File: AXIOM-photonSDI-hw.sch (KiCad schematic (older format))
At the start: 4 parts, among them J101 Conn_Coaxial, J102 Conn_Coaxial, J103 Conn_Coaxial, J104 Conn_Coaxial

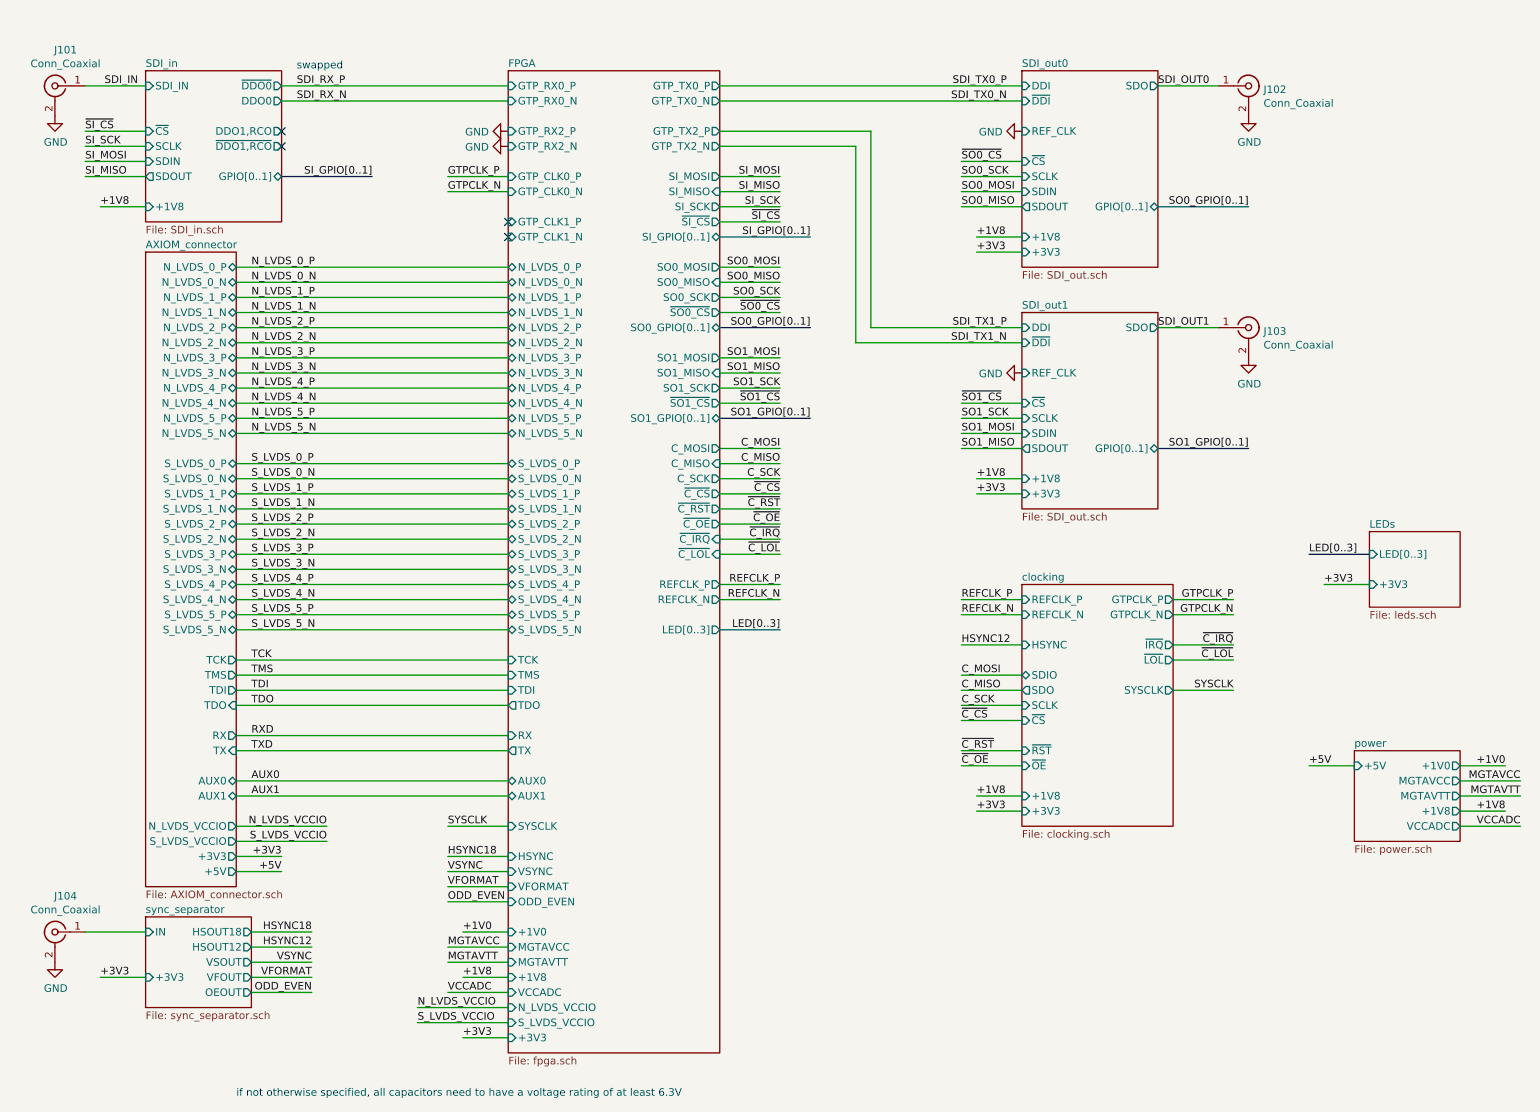
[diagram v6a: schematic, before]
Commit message: fix moved plane bug, add init, done and power enable signals and optimize design
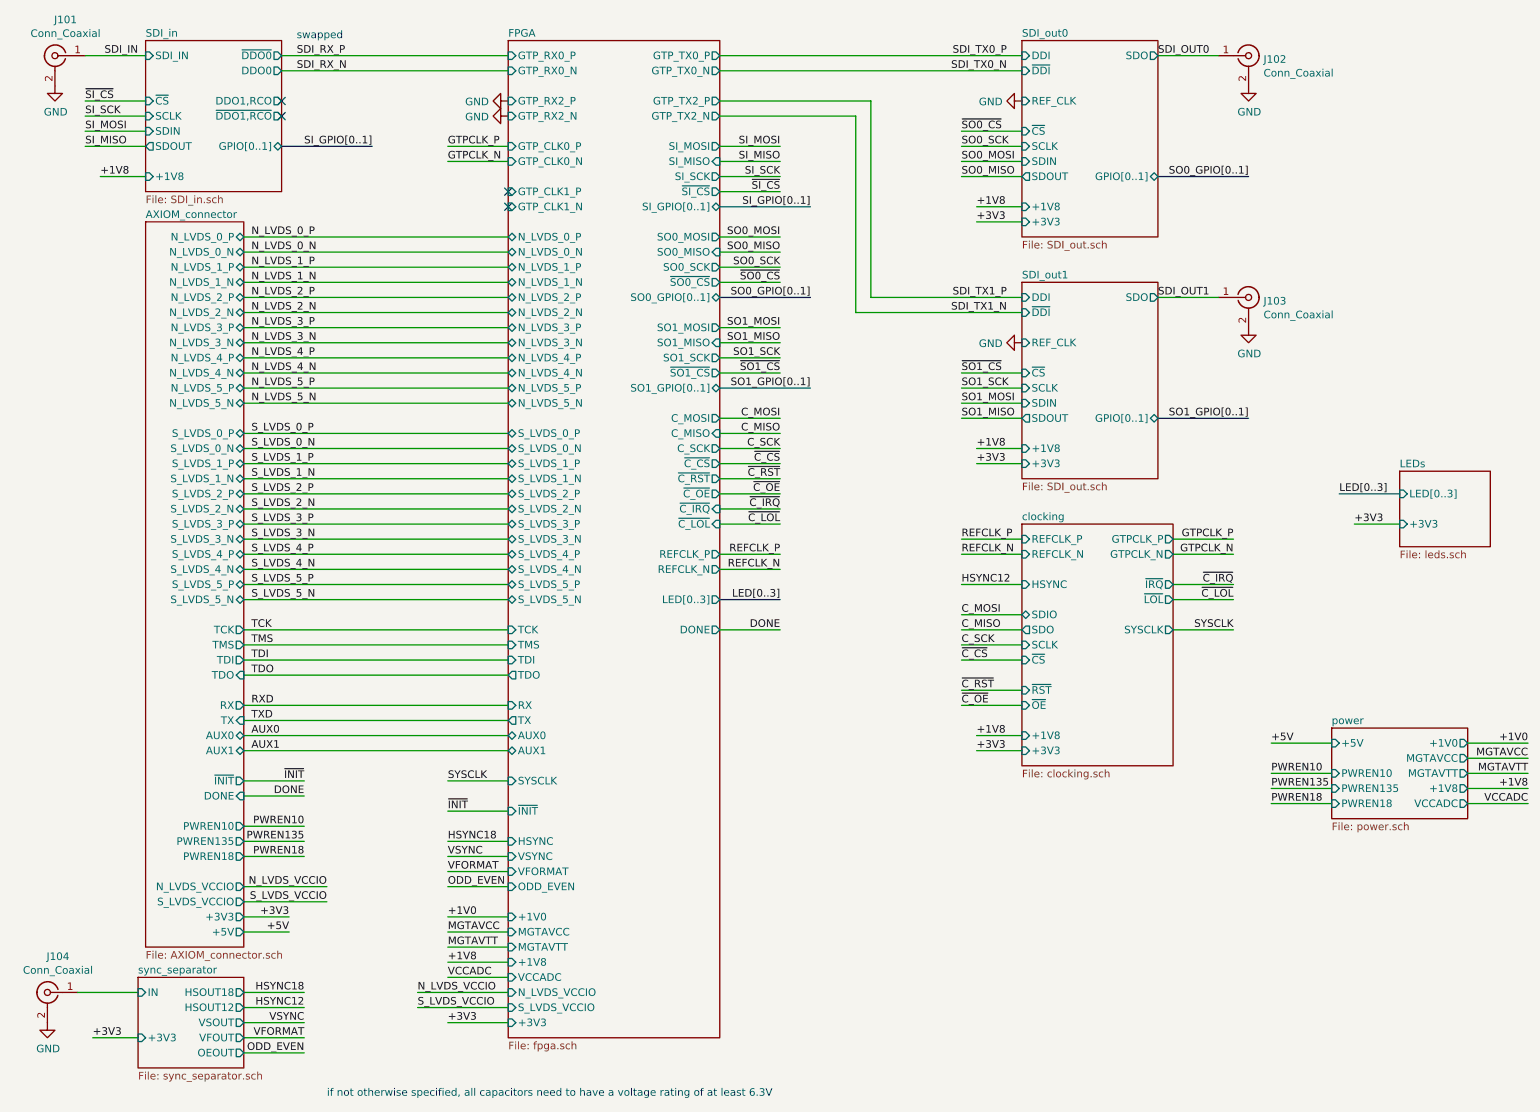
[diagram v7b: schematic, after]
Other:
- moved on the sheet: J101, J102, J103, J104
